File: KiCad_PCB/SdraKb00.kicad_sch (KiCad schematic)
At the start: 75 parts, among them J2 AVR-ISP-6, SW03 RotaryEncoder_Switch, SW1 Reset_SW, U2 PRTR5V0U2X, U3 ATmega32U4-A, Y1 16MHz

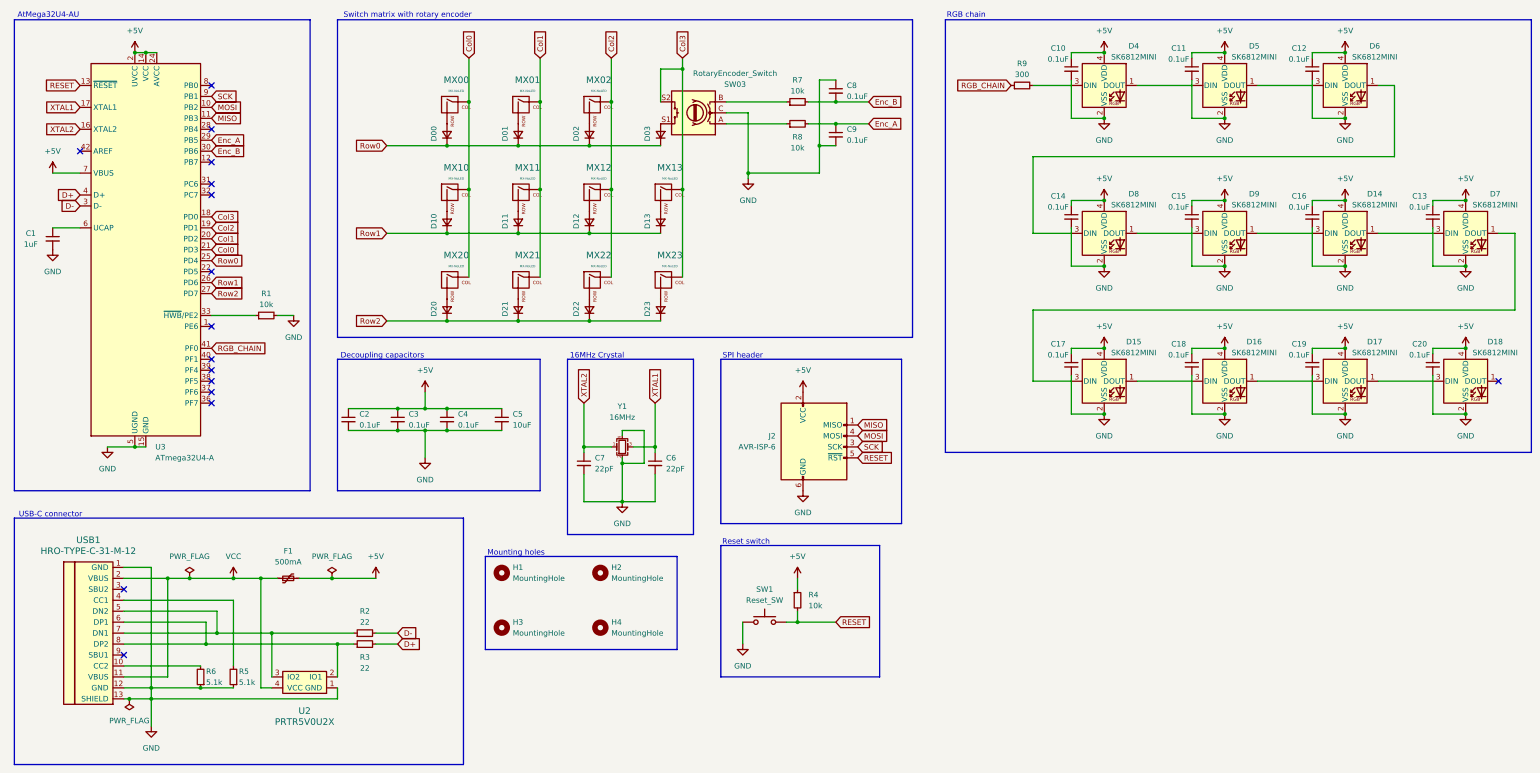
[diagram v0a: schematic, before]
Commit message: Assign footprints (#3)
* First round assigning footprints.

* Complete footprint assignment.

- Removed unused submodules
- Adding marbastlib submodule
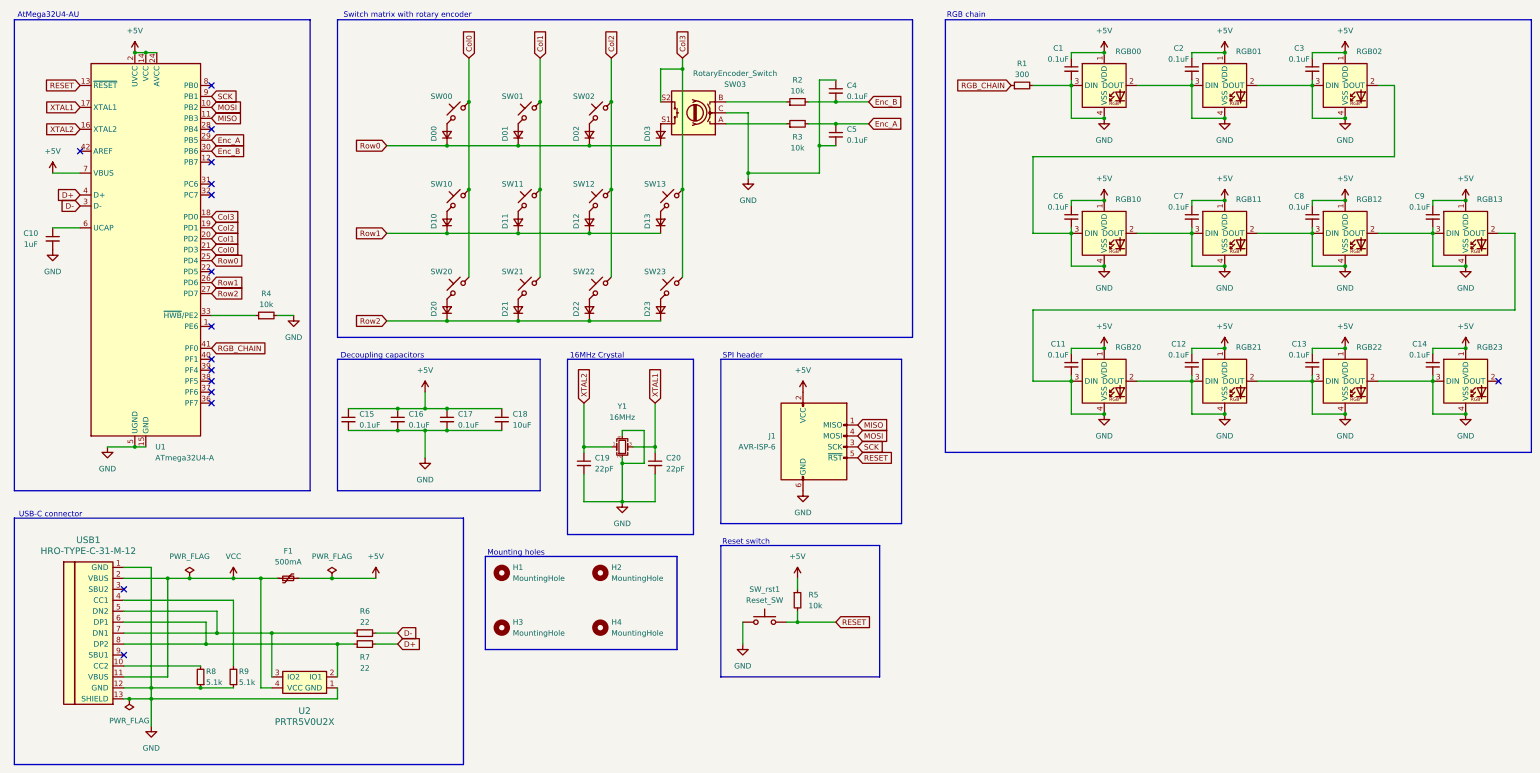
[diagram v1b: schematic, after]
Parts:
- removed D14, D15, D16, D17, D18, D4, D5, D6, D7, D8, D9: SK6812MINI, LED_SMD:LED_SK6812MINI_PLCC4_3.5x3.5mm_P1.75mm, symbol LED:SK6812MINI
- removed MX00, MX01, MX02, MX10, MX11, MX12, MX13, MX20, MX21, MX22, MX23: MX-NoLED, symbol MX_Alps_Hybrid:MX-NoLED
- added RGB00, RGB01, RGB02, RGB10, RGB11, RGB12, RGB13, RGB20, RGB21, RGB22, RGB23: MX_SK6812MINI-E, marbastlib-mx:LED_MX_6028R, symbol marbastlib-mx:MX_SK6812MINI-E
- added SW00, SW01, SW02, SW10, SW11, SW12, SW13, SW20, SW21, SW22, SW23: SW_Push_45deg, marbastlib-mx:SW_MX_HS_CPG151101S11_1u, symbol Switch:SW_Push_45deg
- C1: renamed from C10; footprint (none) -> Capacitor_SMD:C_0805_2012Metric_Pad1.18x1.45mm_HandSolder
- C10: renamed from C1; footprint (none) -> Capacitor_SMD:C_0805_2012Metric_Pad1.18x1.45mm_HandSolder
- C11: renamed from C17; footprint (none) -> Capacitor_SMD:C_0805_2012Metric_Pad1.18x1.45mm_HandSolder
- C12: renamed from C18; footprint (none) -> Capacitor_SMD:C_0805_2012Metric_Pad1.18x1.45mm_HandSolder
- C13: renamed from C19; footprint (none) -> Capacitor_SMD:C_0805_2012Metric_Pad1.18x1.45mm_HandSolder
- C14: renamed from C20; footprint (none) -> Capacitor_SMD:C_0805_2012Metric_Pad1.18x1.45mm_HandSolder
- C15: renamed from C2; footprint (none) -> Capacitor_SMD:C_0805_2012Metric_Pad1.18x1.45mm_HandSolder
- C16: renamed from C3; footprint (none) -> Capacitor_SMD:C_0805_2012Metric_Pad1.18x1.45mm_HandSolder
- C17: renamed from C4; footprint (none) -> Capacitor_SMD:C_0805_2012Metric_Pad1.18x1.45mm_HandSolder
- C18: renamed from C5; footprint (none) -> Capacitor_SMD:C_0805_2012Metric_Pad1.18x1.45mm_HandSolder
- C19: renamed from C7; footprint (none) -> Capacitor_SMD:C_0805_2012Metric_Pad1.18x1.45mm_HandSolder
- C2: renamed from C11; footprint (none) -> Capacitor_SMD:C_0805_2012Metric_Pad1.18x1.45mm_HandSolder
- C20: renamed from C6; footprint (none) -> Capacitor_SMD:C_0805_2012Metric_Pad1.18x1.45mm_HandSolder
- C3: renamed from C12; footprint (none) -> Capacitor_SMD:C_0805_2012Metric_Pad1.18x1.45mm_HandSolder
- C4: renamed from C8; footprint (none) -> Capacitor_SMD:C_0805_2012Metric_Pad1.18x1.45mm_HandSolder
- C5: renamed from C9; footprint (none) -> Capacitor_SMD:C_0805_2012Metric_Pad1.18x1.45mm_HandSolder
- C6: renamed from C14; footprint (none) -> Capacitor_SMD:C_0805_2012Metric_Pad1.18x1.45mm_HandSolder
- C7: renamed from C15; footprint (none) -> Capacitor_SMD:C_0805_2012Metric_Pad1.18x1.45mm_HandSolder
- C8: renamed from C16; footprint (none) -> Capacitor_SMD:C_0805_2012Metric_Pad1.18x1.45mm_HandSolder
- C9: renamed from C13; footprint (none) -> Capacitor_SMD:C_0805_2012Metric_Pad1.18x1.45mm_HandSolder
- D00, D01, D02, D03, D10, D11, D12, D13, D20, D21, D22, D23: footprint (none) -> Diode_SMD:D_SOD-123
- F1: footprint (none) -> Fuse:Fuse_1206_3216Metric_Pad1.42x1.75mm_HandSolder
- H1, H2, H3, H4: footprint (none) -> MountingHole:MountingHole_3.2mm_M3
- J1: renamed from J2; footprint (none) -> Connector_IDC:IDC-Header_2x03_P2.54mm_Vertical
- R1: renamed from R9; footprint (none) -> Resistor_SMD:R_0805_2012Metric_Pad1.20x1.40mm_HandSolder
- R2: renamed from R7; footprint (none) -> Resistor_SMD:R_0805_2012Metric_Pad1.20x1.40mm_HandSolder
- R3: renamed from R8; footprint (none) -> Resistor_SMD:R_0805_2012Metric_Pad1.20x1.40mm_HandSolder
- R4: renamed from R1; footprint (none) -> Resistor_SMD:R_0805_2012Metric_Pad1.20x1.40mm_HandSolder
- R5: renamed from R4; footprint (none) -> Resistor_SMD:R_0805_2012Metric_Pad1.20x1.40mm_HandSolder
- R6: renamed from R2; footprint (none) -> Resistor_SMD:R_0805_2012Metric_Pad1.20x1.40mm_HandSolder
- R7: renamed from R3; footprint (none) -> Resistor_SMD:R_0805_2012Metric_Pad1.20x1.40mm_HandSolder
- R8: renamed from R6; footprint (none) -> Resistor_SMD:R_0805_2012Metric_Pad1.20x1.40mm_HandSolder
- R9: renamed from R5; footprint (none) -> Resistor_SMD:R_0805_2012Metric_Pad1.20x1.40mm_HandSolder
- SW03: footprint (none) -> marbastlib-various:ROT_Alps_EC11E-Switch
- SW_rst1: renamed from SW1; footprint (none) -> Button_Switch_SMD:SW_SPST_SKQG_WithStem
- U2: footprint (none) -> Package_TO_SOT_SMD:SOT-143_Handsoldering
- USB1: footprint (none) -> Type-C:HRO-TYPE-C-31-M-12-HandSoldering
- Y1: footprint (none) -> Crystal:Crystal_SMD_3225-4Pin_3.2x2.5mm_HandSoldering
- renumbered U3 to U1
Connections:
- net +5V: now also RGB00.1 (VDD), RGB01.1 (VDD), RGB02.1 (VDD), RGB10.1 (VDD), RGB11.1 (VDD), RGB12.1 (VDD), RGB13.1 (VDD), RGB20.1 (VDD), RGB21.1 (VDD), RGB22.1 (VDD), RGB23.1 (VDD)
- net Col0: now also SW00.2, SW10.2, SW20.2
- net Col1: now also SW01.2, SW11.2, SW21.2
- net Col2: now also SW02.2, SW12.2, SW22.2
- net Col3: now also SW13.2, SW23.2
- net GND: now also R1.2, RGB00.2 (DOUT), RGB00.3 (DIN), RGB00.4 (VSS), RGB01.2 (DOUT), RGB01.3 (DIN), RGB01.4 (VSS), RGB02.2 (DOUT), RGB02.3 (DIN), RGB02.4 (VSS), RGB10.2 (DOUT), RGB10.3 (DIN), RGB10.4 (VSS), RGB11.2 (DOUT), RGB11.3 (DIN), RGB11.4 (VSS), RGB12.2 (DOUT), RGB12.3 (DIN), RGB12.4 (VSS), RGB13.2 (DOUT), RGB13.3 (DIN), RGB13.4 (VSS), RGB20.2 (DOUT), RGB20.3 (DIN), RGB20.4 (VSS), RGB21.2 (DOUT), RGB21.3 (DIN), RGB21.4 (VSS), RGB22.2 (DOUT), RGB22.3 (DIN), RGB22.4 (VSS), RGB23.3 (DIN), RGB23.4 (VSS)
- net at D11.2 (A): now also SW11.1
- net at D01.2 (A): now also SW01.1
- net at D21.2 (A): now also SW21.1
- net at D23.2 (A): now also SW23.1
- net at D00.2 (A): now also SW00.1
- net at D20.2 (A): now also SW20.1
- net at D12.2 (A): now also SW12.1
- net at D10.2 (A): now also SW10.1
- net at D22.2 (A): now also SW22.1
- net at D13.2 (A): now also SW13.1
- net at D02.2 (A): now also SW02.1

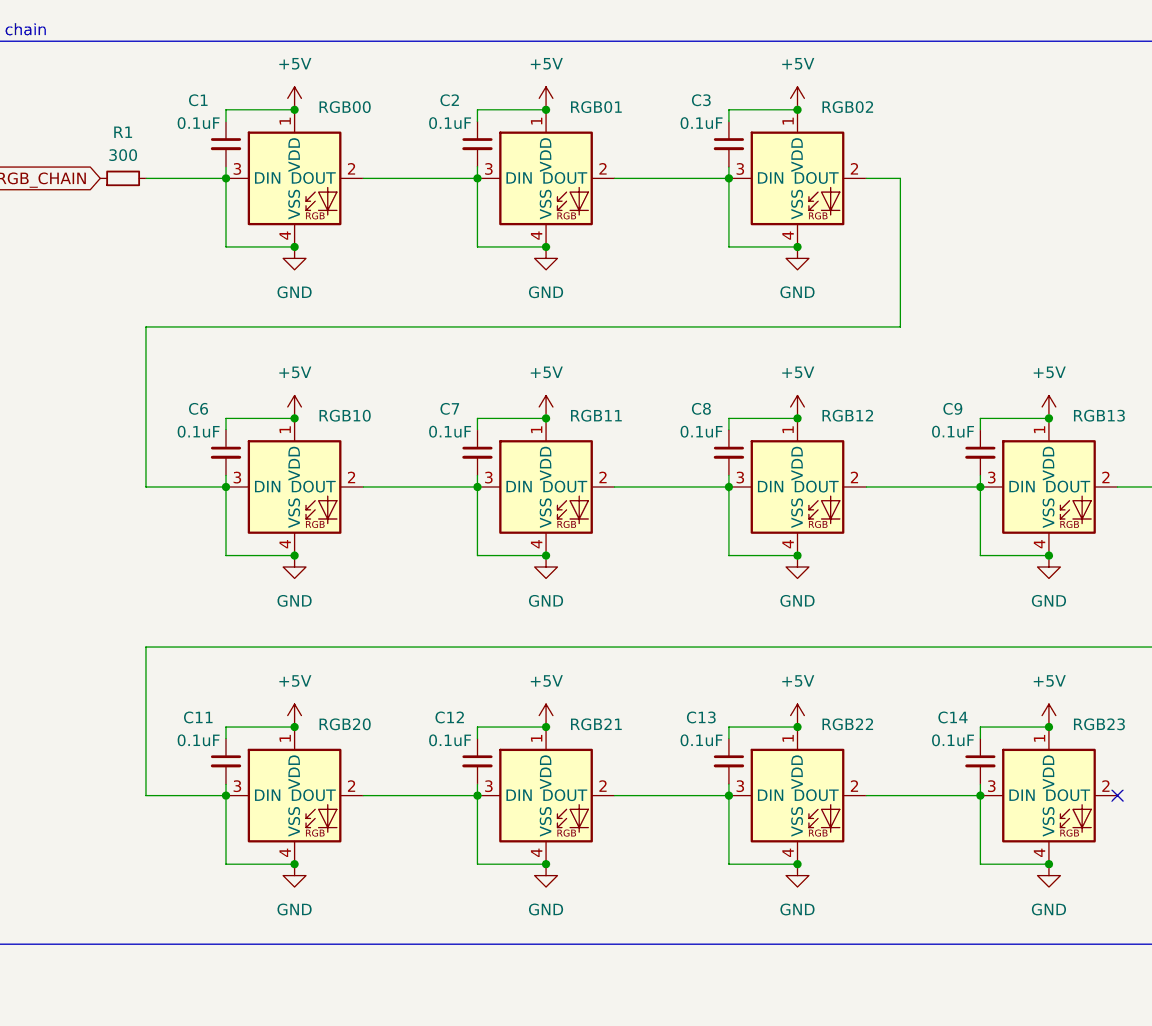
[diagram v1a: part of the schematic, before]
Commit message: Aligning SWs, Ds, LEDs.
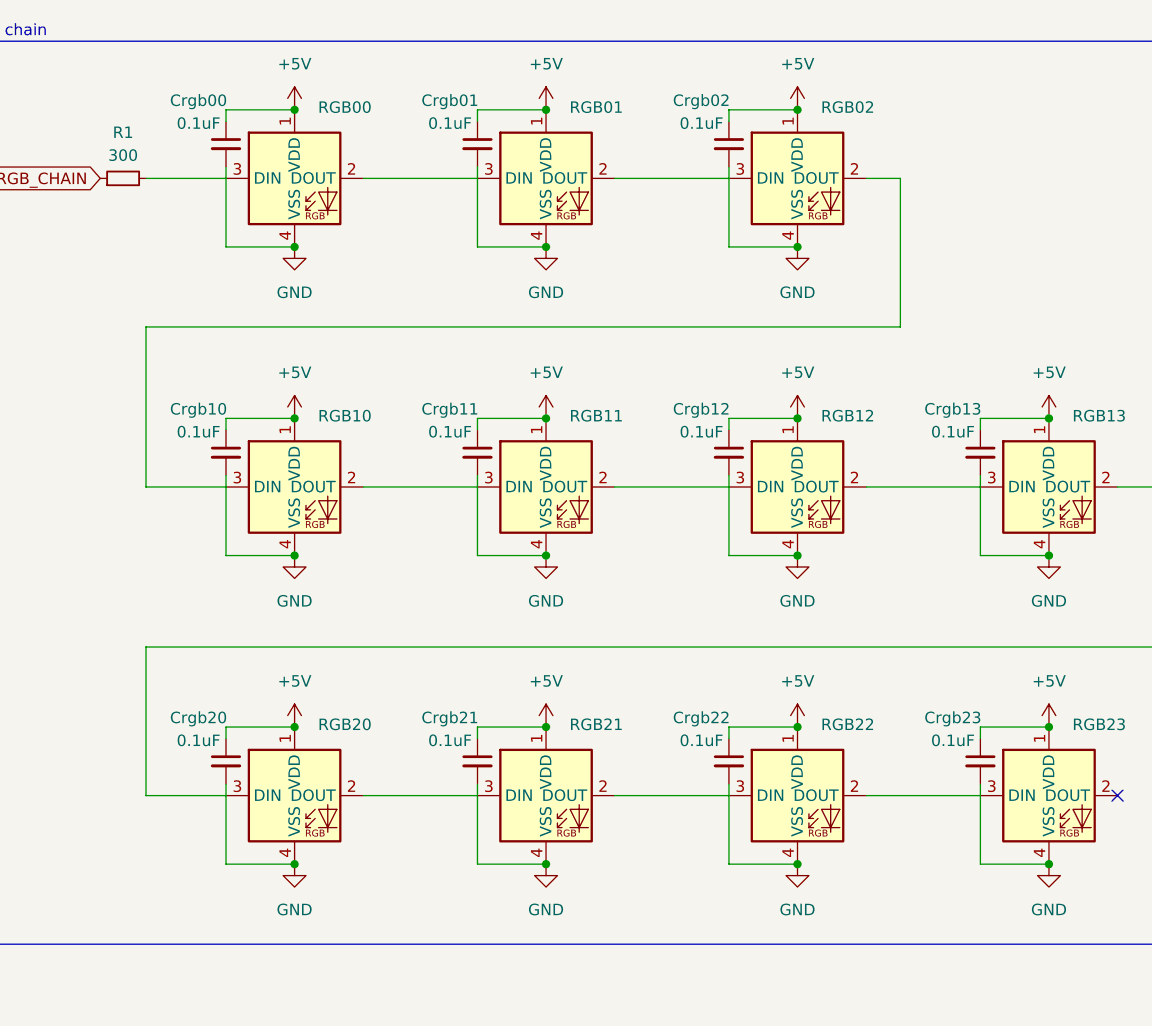
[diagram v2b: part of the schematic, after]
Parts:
- RGB00, RGB01, RGB02, RGB10, RGB11, RGB12, RGB13, RGB20, RGB21, RGB22, RGB23: footprint marbastlib-mx:LED_MX_6028R -> marbastlib-mx:LED_MX_6028R-ROT
- renumbered C1 to Crgb00, C2 to Crgb01, C3 to Crgb02, C6 to Crgb10, C7 to Crgb11, C8 to Crgb12, C9 to Crgb13, C11 to Crgb20, C12 to Crgb21, C13 to Crgb22, C14 to Crgb23
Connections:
- net GND: no longer R1.2, RGB00.2 (DOUT), RGB00.3 (DIN), RGB01.2 (DOUT), RGB01.3 (DIN), RGB02.2 (DOUT), RGB02.3 (DIN), RGB10.2 (DOUT), RGB10.3 (DIN), RGB11.2 (DOUT), RGB11.3 (DIN), RGB12.2 (DOUT), RGB12.3 (DIN), RGB13.2 (DOUT), RGB13.3 (DIN), RGB20.2 (DOUT), RGB20.3 (DIN), RGB21.2 (DOUT), RGB21.3 (DIN), RGB22.2 (DOUT), RGB22.3 (DIN), RGB23.3 (DIN)
- new net: RGB10.2 (DOUT), RGB11.3 (DIN)
- new net: RGB02.2 (DOUT), RGB10.3 (DIN)
- new net: RGB00.2 (DOUT), RGB01.3 (DIN)
- new net: R1.2, RGB00.3 (DIN)
- new net: RGB22.2 (DOUT), RGB23.3 (DIN)
- new net: RGB21.2 (DOUT), RGB22.3 (DIN)
- new net: RGB11.2 (DOUT), RGB12.3 (DIN)
- new net: RGB12.2 (DOUT), RGB13.3 (DIN)
- new net: RGB13.2 (DOUT), RGB20.3 (DIN)
- new net: RGB01.2 (DOUT), RGB02.3 (DIN)
- new net: RGB20.2 (DOUT), RGB21.3 (DIN)

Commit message: More wiring.
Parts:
- J1: footprint Connector_IDC:IDC-Header_2x03_P2.54mm_Vertical -> Connector_PinHeader_2.00mm:PinHeader_1x06_P2.00mm_Vertical
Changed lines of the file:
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@@
 			)
 		)
-		(property "Footprint" "Connector_IDC:IDC-Header_2x03_P2.54mm_Vertical"
+		(property "Footprint" "Connector_PinHeader_2.00mm:PinHeader_1x06_P2.00mm_Vertical"
 			(at 201.93 119.38 90)
 			(effects

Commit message: More PCB routing.
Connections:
- net DN: now reaches R7.1, U2.2 (IO1), USB1.6 (DP1), USB1.8 (DP2)
- net DP: now reaches R6.1, U2.3 (IO2), USB1.5 (DN2), USB1.7 (DN1)
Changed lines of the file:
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@@
+		)
+	)
+	(global_label "DP"
+		(shape input)
+		(at 90.17 163.83 90)
+		(fields_autoplaced yes)
+		(effects
+			(font
+				(size 1.27 1.27)
+			)
+			(justify left)
+		)
+		(property "Intersheetrefs" "${INTERSHEET_REFS}"
+			(at 90.17 158.3048 90)
+			(effects
+				(font
+					(size 1.27 1.27)
+				)
+				(justify left)
+				(hide yes)
+			)
 		)
 	)
@@
 			(effects
 				(font
+					(size 1.27 1.27)
+				)
+				(justify right)
+				(hide yes)
+			)
+		)
+	)
+	(global_label "DN"
+		(shape input)
+		(at 90.17 166.37 270)
+		(fields_autoplaced yes)
+		(effects
+			(font
+				(size 1.27 1.27)
+			)
+			(justify right)
+		)
+		(property "Intersheetrefs" "${INTERSHEET_REFS}"
+			(at 90.17 171.9557 90)
+			(effects
+				(font

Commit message: Routing MCU powerlines, Crystal ground zone.
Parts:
- J1: footprint Connector_PinHeader_2.00mm:PinHeader_1x06_P2.00mm_Vertical -> Connector_PinHeader_2.00mm:PinHeader_1x06_P2.00mm_Horizontal
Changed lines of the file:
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@@
 			)
 		)
-		(property "Footprint" "Connector_PinHeader_2.00mm:PinHeader_1x06_P2.00mm_Vertical"
+		(property "Footprint" "Connector_PinHeader_2.00mm:PinHeader_1x06_P2.00mm_Horizontal"
 			(at 201.93 119.38 90)
 			(effects
